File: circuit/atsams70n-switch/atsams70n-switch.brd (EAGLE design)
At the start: 176.5 x 171.7 mm, 72 parts, among them J5 CONN_20X2, Q1 20MHz, U1 REGULATOR_SOT223, U2 ATSAMS70N-TQFP100, U3 ISL3177E, U4 ISL3177E, U5 ISL3177E, U6 ISL3177E, X1 MICRO-USB_1/100

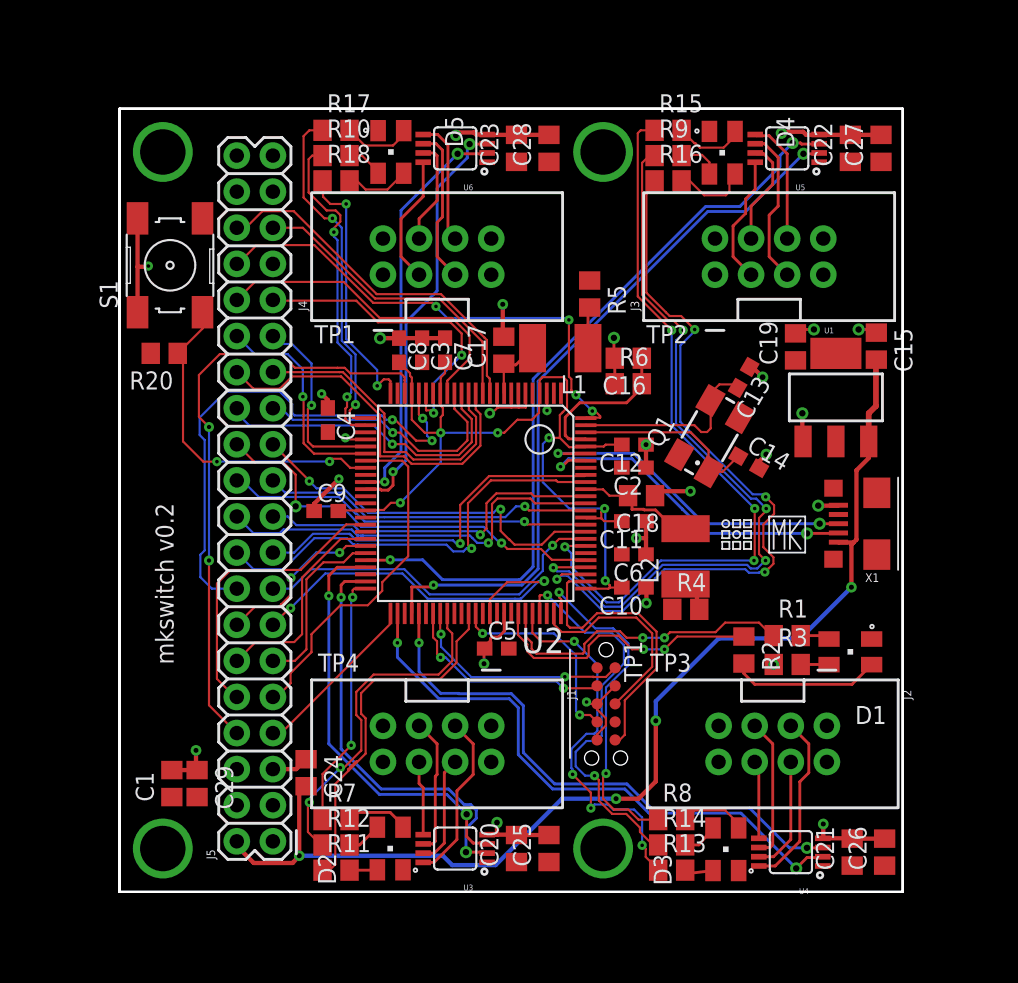
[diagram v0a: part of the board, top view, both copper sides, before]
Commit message: new boards to house
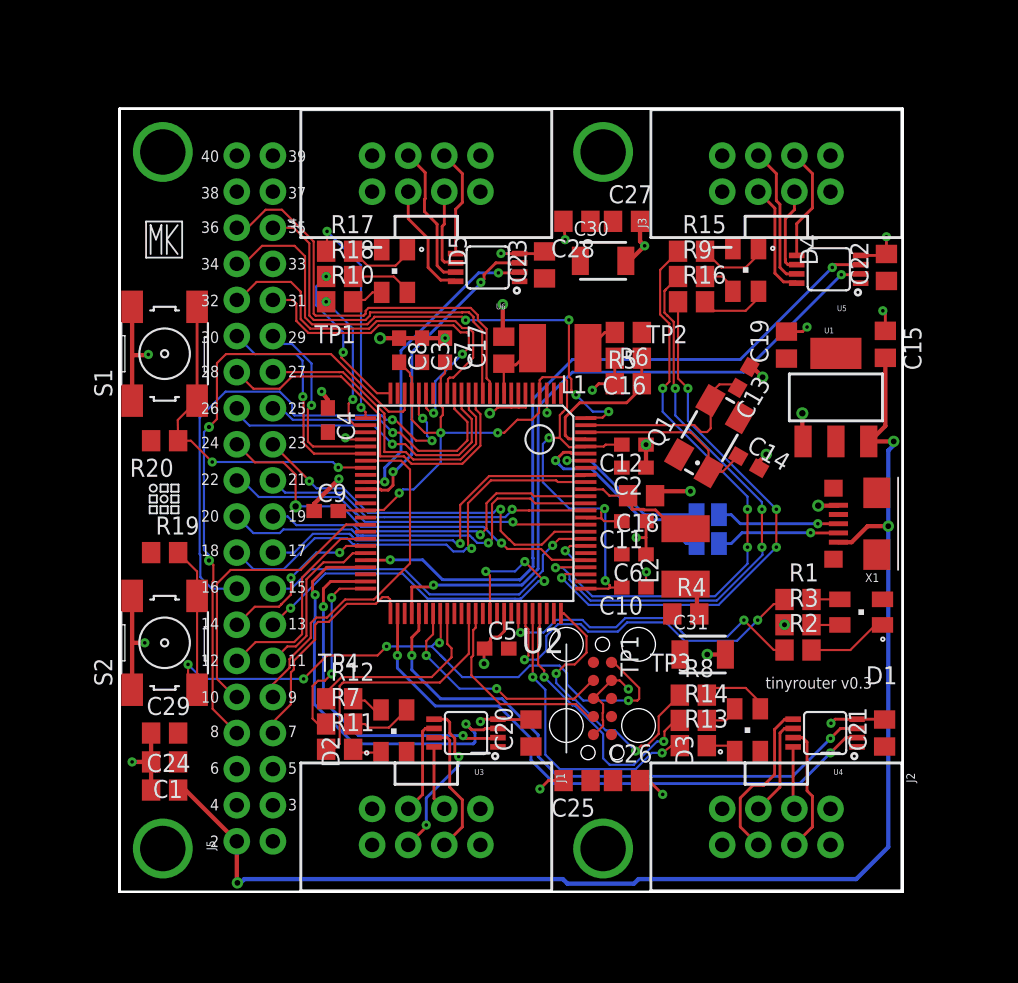
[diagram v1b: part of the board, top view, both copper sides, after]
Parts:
- added C30, C31: 47uF, borkedlabs-passives:1210
- added R19: 10K, eagle-ltspice:R0805
- added S2: (no value), fab:6MM_SWITCH
- added U$3, U$4: SOLDER_JUMPER, fab:SJFAB
- J5: value CONN_20X2 -> CONN_20X2NOSILK; device SparkFun-Connectors:2X20 -> SparkFun-Connectors:2X20_NOSILK
- TP1: value TC2050-MCP-NL -> TC2050-NL; device tag-connect-2050:TC2030-MCP-NL -> tag-connect-2050:TC2050-MCP
- moved U$1 48.5 mm to (11.8, 57.6)
- moved U$2 40.4 mm to (11.8, 39.3)
- moved C26 18.8 mm to (44.3, 19.5), turned to 0 degrees
- moved C27 18.6 mm to (44.3, 58.9), turned to 0 degrees
- moved R10 10.3 mm to (24.1, 53.2)
- moved R12 10.3 mm to (24.1, 25.3)
- moved C24 10.0 mm to (11.8, 18.8), turned to 0 degrees
- moved U5 9.00 mm to (58.5, 55.5)
- moved R8 8.89 mm to (49.0, 25.5)
- moved R13 8.89 mm to (49.0, 22.0)
- moved R14 8.89 mm to (49.0, 23.7)
- moved C22 8.76 mm to (62.6, 55.6)
- moved U4 8.72 mm to (58.3, 22.9)
- moved C21 8.69 mm to (62.5, 22.9)
- moved U6 8.69 mm to (34.5, 55.6)
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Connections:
- new net N$40: U$3.1, X1.D+
- new net N$6: U$4.1, X1.D-
- net +3V3: now also C30.1, C31.1, R19.1
- net DM: now also U$3.2; no longer X1.D-
- net DP: now also U$4.2; no longer X1.D+
- net GND: now also C30.2, C31.2, S2.1, S2.2
- net RESET: now also R19.2, S2.3, S2.4
- net TDI: no longer TP1.8
- net TDO: no longer TP1.6
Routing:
- net RESET: track 15.8 -> 54.8 mm, vias 2 -> 5
- net TDO: track 20.7 -> 0.00 mm
- net +5V: track 79.1 -> 96.7 mm, vias 4 -> 3
- net TDI: track 14.8 -> 0.00 mm
- net P2LG: track 53.4 -> 39.6 mm
- net P1LB: track 23.1 -> 10.5 mm
- net DM: track 24.0 -> 12.0 mm, vias 2 -> 1
- net P2LB: track 53.9 -> 42.1 mm
- net P4LG: track 24.3 -> 13.5 mm, vias 2 -> 0
- net P2LR: track 53.0 -> 42.9 mm
- net P4LR: track 27.3 -> 18.1 mm
- net DP: track 23.8 -> 15.0 mm, vias 2 -> 1
- net N$6: track 0.00 -> 8.73 mm, vias 0 -> 1
- net N$40: track 0.00 -> 8.67 mm, vias 0 -> 1
- net P1LR: track 24.3 -> 15.7 mm
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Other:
- board text added: "10"
- board text added: "11"
- board text added: "12"
- board text added: "13"
- board text added: "14"
- board text added: "15"
- board text added: "16"
- board text added: "17"
- board text added: "18"
- board text added: "19"
- board text added: "2"
- board text added: "20"
- board text added: "21"
- board text added: "22"
- board text added: "23"
- board text added: "24"
- board text added: "25"
- board text added: "26"
- board text added: "27"
- board text added: "28"
- board text added: "29"
- board text added: "3"
- board text added: "30"
- board text added: "31"
- board text added: "32"
- board text added: "33"
- board text added: "34"
- board text added: "35"
- board text added: "36"
- board text added: "37"
- board text added: "38"
- board text added: "39"
- board text added: "4"
- board text added: "40"
- board text added: "5"
- board text added: "6"
- board text added: "7"
- board text added: "8"
- board text added: "9"
- board text added: "tinyrouter v0.3"
- board text removed: "mkswitch v0.2"
